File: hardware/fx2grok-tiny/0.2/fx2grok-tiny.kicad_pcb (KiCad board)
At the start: 2 copper layers, 13 x 13 mm, 27 parts, among them IC1 CY7C68013A-56, P1 CONN_01X05, P2 CONN_01X05, U1 MICRO-USB-B-SMD, U2 MIC5504, Y1 24MHz

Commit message: fx2grok-tiny: Fix incorrect FX2 footprint.
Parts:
- IC1: footprint QFN56 -> fx2grok-tiny:QFN56
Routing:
- net +3V3: track 56.9 -> 49.1 mm
- net /WAKEUP: track 2.63 -> 6.46 mm
- net /SDA: track 3.19 -> 6.34 mm
- net /PA0: track 1.45 -> 4.57 mm, vias 0 -> 2
- net GND: track 79.0 -> 77.8 mm, vias 9 -> 7
- net /SCL: track 3.23 -> 2.08 mm
- net /PB5: track 2.76 -> 3.09 mm, vias 0 -> 1
- net /PB2: track 2.67 -> 2.35 mm, vias 1 -> 0
- net /PB6: track 2.61 -> 2.92 mm, vias 1 -> 0
- net /PB1: track 3.07 -> 2.76 mm, vias 0 -> 1
- net /PB7: track 4.46 -> 4.48 mm, vias 0 -> 1
- net /PB0: track 2.79 -> 2.77 mm, vias 1 -> 0

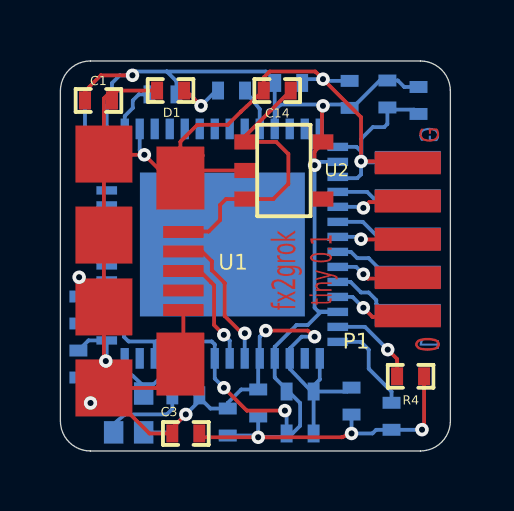
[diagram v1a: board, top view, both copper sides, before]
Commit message: fx2grok-tiny: Reroute PCB from scratch with various changes.
 - The previously incorrect FX2 footprint is fixed now.

 - The FX2's thermal pad is set to GND now.

 - The FX2 footprint now has a dot on the copper as well as on the
   silkscreen for pin 1.

 - The PCB is now 11x11mm (instead of 13x13mm).

 - The 1.27mm pin header connectors are shortened and the pinout changed.

 - The trace clearance changed from 6mil to 5mil.

 - The USB connector footprint now has two oval pads (space reasons).

 - The LED is now connected to PA1 (not PA0).

 - The schematics/layout license is changed to CC-BY-SA 4.0.
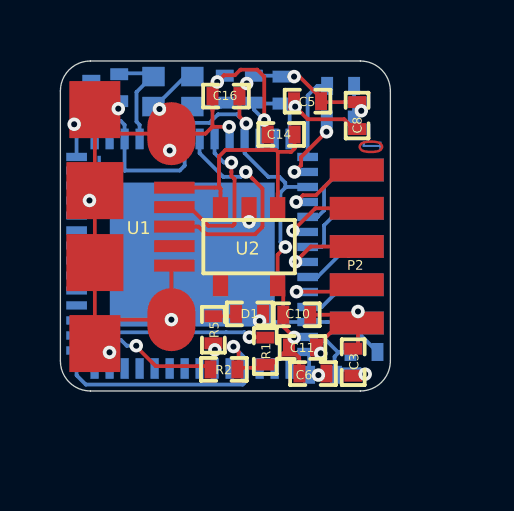
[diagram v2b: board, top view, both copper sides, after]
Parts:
- C1, R4: moved to B.Cu
- C10, C11, C16, C5, C6, C8, R1, R2, R5: moved to F.Cu
- P1: footprint fx2grok-tiny:CONN-5x1-SMD-127MM -> CONN-5x1-SMD-127MM; moved to B.Cu
- P2: footprint fx2grok-tiny:CONN-5x1-SMD-127MM -> CONN-5x1-SMD-127MM; moved to F.Cu
- U1: footprint fx2grok-tiny:MICRO-USB-B-SMD -> MICRO-USB-B-SMD
- moved C2 12.1 mm to (68.7, 38.9), turned to 90 degrees
- moved R3 11.1 mm to (77.0, 38.6), turned to 0 degrees
- moved C8 11.1 mm to (77.6, 39.6), turned to 270 degrees
- moved Y1 10.8 mm to (71.5, 38.8), turned to 180 degrees
- moved C4 10.3 mm to (73.2, 38.7), turned to 90 degrees
- moved R1 10.0 mm to (74.5, 47.4), turned to 90 degrees
- moved C12 9.62 mm to (77.8, 47.4), turned to 0 degrees
- moved R2 9.39 mm to (73.2, 48.0)
- moved C9 9.31 mm to (69.7, 38.6), turned to 270 degrees
- moved R4 8.88 mm to (77.0, 39.7)
- moved R5 8.00 mm to (72.8, 46.7), turned to 90 degrees
- moved C10 7.96 mm to (75.6, 46.2), turned to 0 degrees
- moved D1 7.90 mm to (74.0, 46.2)
- moved C16 6.42 mm to (73.2, 38.9), turned to 180 degrees
- moved C3 6.06 mm to (77.5, 47.8), turned to 90 degrees
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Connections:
- D1 pad 1: Net-(D1-Pad1) -> GND
- D1 pad 2: GND -> Net-(D1-Pad2)
- IC1 pad 33: /PA0 -> (no net)
- IC1 pad 34: (no net) -> /PA1
- P1 pad 1: /PB0 -> /PB1
- P1 pad 2: /PB2 -> /PB3
- P1 pad 3: /PB4 -> /PB5
- P1 pad 4: /PB6 -> /PB7
- P2 pad 2: /PB7 -> /PB6
- P2 pad 3: /PB5 -> /PB4
- P2 pad 4: /PB3 -> /PB2
- P2 pad 5: /PB1 -> /PB0
- R5 pad 1: Net-(D1-Pad1) -> /PA1
- R5 pad 2: /PA0 -> Net-(D1-Pad2)
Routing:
- net GND: track 77.8 -> 53.5 mm, vias 7 -> 16
- net +3V3: track 49.1 -> 44.4 mm
- net /PA0: track 4.57 -> 0.00 mm, vias 2 -> 0
- net /DP: track 3.88 -> 7.61 mm
- net /SDA: track 6.34 -> 2.75 mm, vias 1 -> 2
- net /RESET#: track 1.88 -> 5.05 mm, vias 0 -> 1
- net /PB7: track 4.48 -> 2.43 mm, vias 1 -> 0
- net Net-(D1-Pad1): track 1.44 -> 0.00 mm, vias 1 -> 0
- net /PB4: track 2.68 -> 3.96 mm
- net /XTALIN: track 4.28 -> 3.12 mm
- net /PB2: track 2.35 -> 3.36 mm, vias 0 -> 1
- net +5V: track 9.48 -> 8.48 mm
- net /PA1: track 0.00 -> 0.87 mm, vias 0 -> 1
- net Net-(D1-Pad2): track 0.00 -> 0.79 mm
- net /SCL: track 2.08 -> 2.83 mm
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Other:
- board size 13 x 13 mm -> 11 x 11 mm
- net class Default: clearance 0.1524 -> 0.127
- rule trace_clearance: 0.1524 -> 0.127
- board text added: "."
- board text removed: "G"
- board text removed: "fx2grok"
- board text removed: "tiny 0.1"

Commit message: fx2grok-tiny: Random cosmetic/silkscreen changes.
These are mostly done for being able to generate nice 3D previews in
KiCad that can be helpful for assembling the device.
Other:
- board text added: "GND"
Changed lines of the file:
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@@
     (area 49.0519 20.05304 86.390762 55.159696)
     (thickness 0.8)
-    (drawings 16)
+    (drawings 17)
     (tracks 380)
     (zones 0)
@@
     (aux_axis_origin 0 0)
     (grid_origin 67.70116 48.7492)
-    (visible_elements FFFFFF19)
+    (visible_elements FFFCFF19)
     (pcbplotparams
       (layerselection 0x010cc_80000001)
@@
       (effects (font (size 0.3048 0.3048) (thickness 0.0762)))
     )
-    (fp_text value 100nF (at -0.038 0.022) (layer F.SilkS) hide
+    (fp_text value 100nF (at 0.7 -0.64) (layer F.SilkS)
       (effects (font (size 0.2048 0.2048) (thickness 0.0512)))
     )
@@
       (effects (font (size 0.3048 0.3048) (thickness 0.0762)))
     )
-    (fp_text value 1uF (at 0.04064 0 180) (layer F.SilkS) hide
+    (fp_text value 1uF (at -0.01 -0.69 180) (layer F.SilkS)
       (effects (font (size 0.2048 0.2048) (thickness 0.0512)))
     )
@@
       (effects (font (size 0.3048 0.3048) (thickness 0.0762)))
     )
-    (fp_text value 100nF (at -0.0254 -0.03556 180) (layer F.SilkS) hide
+    (fp_text value 100nF (at -0.27 0.65 180) (layer F.SilkS)
       (effects (font (size 0.2048 0.2048) (thickness 0.0512)))
     )
@@
       (effects (font (size 0.3048 0.3048) (thickness 0.0762)))
     )
-    (fp_text value 1uF (at 0 0 180) (layer F.SilkS) hide
+    (fp_text value 1uF (at -0.21 0.66 180) (layer F.SilkS)
       (effects (font (size 0.2048 0.2048) (thickness 0.0512)))
     )
@@
       (effects (font (size 0.3048 0.3048) (thickness 0.0762)) (justify mirror))
     )
-    (fp_text value 100nF (at -0.01524 0 270) (layer B.SilkS) hide
+    (fp_text value 100nF (at -1.54 -0.02 270) (layer B.SilkS)
       (effects (font (size 0.2048 0.2048) (thickness 0.0512)) (justify mirror))
     )
@@
       (effects (font (size 0.3048 0.3048) (thickness 0.0762)))
     )
-    (fp_text value 2K7 (at 0.06604 -0.0254 180) (layer F.SilkS) hide
+    (fp_text value 2K7 (at -0.01 -0.95 180) (layer F.SilkS)
       (effects (font (size 0.2048 0.2048) (thickness 0.0512)))
     )
@@
       (effects (font (size 0.3048 0.3048) (thickness 0.0762)) (justify mirror))
     )
-    (fp_text value 100nF (at 0.01016 0 180) (layer B.SilkS) hide
+    (fp_text value 100nF (at 0.08 -0.79 180) (layer B.SilkS)
       (effects (font (size 0.2048 0.2048) (thickness 0.0512)) (justify mirror))
     )
@@
       (effects (font (size 0.3048 0.3048) (thickness 0.0762)) (justify mirror))
     )
-    (fp_text value 100nF (at -0.04064 0 90) (layer B.SilkS) hide
+    (fp_text value 100nF (at 1.68 0.02 90) (layer B.SilkS)
       (effects (font (size 0.2048 0.2048) (thickness 0.0512)) (justify mirror))
     )
@@
       (effects (font (size 0.3048 0.3048) (thickness 0.0762)) (justify mirror))
     )
-    (fp_text value 100nF (at 0 -0.01524) (layer B.SilkS) hide
+    (fp_text value 100nF (at 0.02 -0.7) (layer B.SilkS)
       (effects (font (size 0.2048 0.2048) (thickness 0.0512)) (justify mirror))
     )
@@
       (effects (font (size 0.3048 0.3048) (thickness 0.0762)))
     )
-    (fp_text value 100nF (at 0.0254 -0.01016) (layer F.SilkS) hide
+    (fp_text value 100nF (at 0.33 -0.53) (layer F.SilkS)
       (effects (font (size 0.2048 0.2048) (thickness 0.0512)))
     )
@@
       (effects (font (size 0.3048 0.3048) (thickness 0.0762)))
     )
-    (fp_text value 2.2uF (at 0.0127 -0.02286) (layer F.SilkS) hide
+    (fp_text value 2.2uF (at 0.02 0.77) (layer F.SilkS)
       (effects (font (size 0.2048 0.2048) (thickness 0.0512)))
     )
@@
     (at 73.18116 38.6892 90)
     (attr smd)
-    (fp_text reference C4 (at -0.24 1.02 90) (layer B.SilkS)
+    (fp_text reference C4 (at 0.01 0.01 90) (layer B.SilkS)
       (effects (font (size 0.3048 0.3048) (thickness 0.0762)) (justify mirror))
     )
-    (fp_text value 12pF (at -0.04064 -0.0254 90) (layer B.SilkS) hide
+    (fp_text value 12pF (at 1.41 -0.04 90) (layer B.SilkS)
       (effects (font (size 0.2048 0.2048) (thickness 0.0512)) (justify mirror))
     )
@@
       (effects (font (size 0.3048 0.3048) (thickness 0.0762)) (justify mirror))
     )
-    (fp_text value 12pF (at 0.02286 -0.01524 270) (layer B.SilkS) hide
+    (fp_text value 12pF (at -1.43 0.04 270) (layer B.SilkS)
       (effects (font (size 0.2048 0.2048) (thickness 0.0512)) (justify mirror))
     )
@@
     (at 74.15116 38.6892 270)
     (attr smd)
-    (fp_text reference C1 (at 0.14 0.88 270) (layer B.SilkS)
+    (fp_text reference C1 (at -0.01 -0.03 270) (layer B.SilkS)
       (effects (font (size 0.3048 0.3048) (thickness 0.0762)) (justify mirror))
     )
-    (fp_text value 1uF (at 0 0 270) (layer B.SilkS) hide
+    (fp_text value 1uF (at -1.39 0.04 270) (layer B.SilkS)
       (effects (font (size 0.2048 0.2048) (thickness 0.0512)) (justify mirror))
     )
@@
       (effects (font (size 0.3048 0.3048) (thickness 0.0762)))
     )
-    (fp_text value 100K (at 0 0 90) (layer F.SilkS) hide
+    (fp_text value 100K (at -1.34 0 90) (layer F.SilkS)
       (effects (font (size 0.2048 0.2048) (thickness 0.0512)))
     )
@@
       (effects (font (size 0.3048 0.3048) (thickness 0.0762)) (justify mirror))
     )
-    (fp_text value 2K7 (at -0.00254 -0.0127) (layer B.SilkS) hide
+    (fp_text value 2K7 (at -0.01 0.87) (layer B.SilkS)
       (effects (font (size 0.2048 0.2048) (thickness 0.0512)) (justify mirror))
     )
@@
       (effects (font (size 0.3048 0.3048) (thickness 0.0762)))
     )
-    (fp_text value 2.2uF (at 0.00254 0.0127 90) (layer F.SilkS) hide
+    (fp_text value 2.2uF (at -1.37 0.02 90) (layer F.SilkS)
       (effects (font (size 0.2048 0.2048) (thickness 0.0512)))
     )
@@
       (effects (font (size 0.3048 0.3048) (thickness 0.0762)))
     )
-    (fp_text value 100nF (at 0 0.01524 270) (layer F.SilkS) hide
+    (fp_text value 100nF (at -1.31042 0 270) (layer F.SilkS)
       (effects (font (size 0.2048 0.2048) (thickness 0.0512)))
     )
@@
       (effects (font (size 0.3048 0.3048) (thickness 0.0762)) (justify mirror))
     )
-    (fp_text value 2K7 (at -0.0127 -0.01016) (layer B.SilkS) hide
+    (fp_text value 2K7 (at -0.09 -1.09) (layer B.SilkS)
       (effects (font (size 0.2048 0.2048) (thickness 0.0512)) (justify mirror))
     )
@@
   (module ABM11 (layer B.Cu)
     (at 71.45116 38.7692 180)
-    (fp_text reference Y1 (at 0.05 0 180) (layer B.SilkS)
+    (fp_text reference Y1 (at 0.18 0.55 180) (layer B.SilkS)
       (effects (font (size 0.424 0.424) (thickness 0.106)) (justify mirror))
     )
@@
       (effects (font (size 0.3048 0.3048) (thickness 0.0762)))
     )
-    (fp_text value 2K7 (at 0 0 90) (layer F.SilkS) hide
+    (fp_text value 2K7 (at 0.03 -0.57 90) (layer F.SilkS)
       (effects (font (size 0.2048 0.2048) (thickness 0.0512)))
     )
@@
       (effects (font (size 0.3048 0.3048) (thickness 0.0762)))
     )
-    (fp_text value LED1 (at 0 0 180) (layer F.SilkS) hide
+    (fp_text value LED1 (at 0 0.66 180) (layer F.SilkS)
       (effects (font (size 0.2048 0.2048) (thickness 0.0512)))
     )
@@
     )
   )
+  (gr_text GND (at 74.54116 46.1492 90) (layer F.SilkS)
+    (effects (font (size 0.127 0.144) (thickness 0.03175)))
+  )
   (gr_text . (at 68.99116 40.5492) (layer B.Mask)
